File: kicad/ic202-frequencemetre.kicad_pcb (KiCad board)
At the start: 2 copper layers, 52 x 48 mm, 49 parts, among them J1 +12V IN (4 pins: 2x+12V, 2x G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, J2 RF IN, J4 LCD, Q1 2SC5551AE-TD-E, U1 AMS1117-5.0, U2 AMS1117 (ADJ), U3 MB506

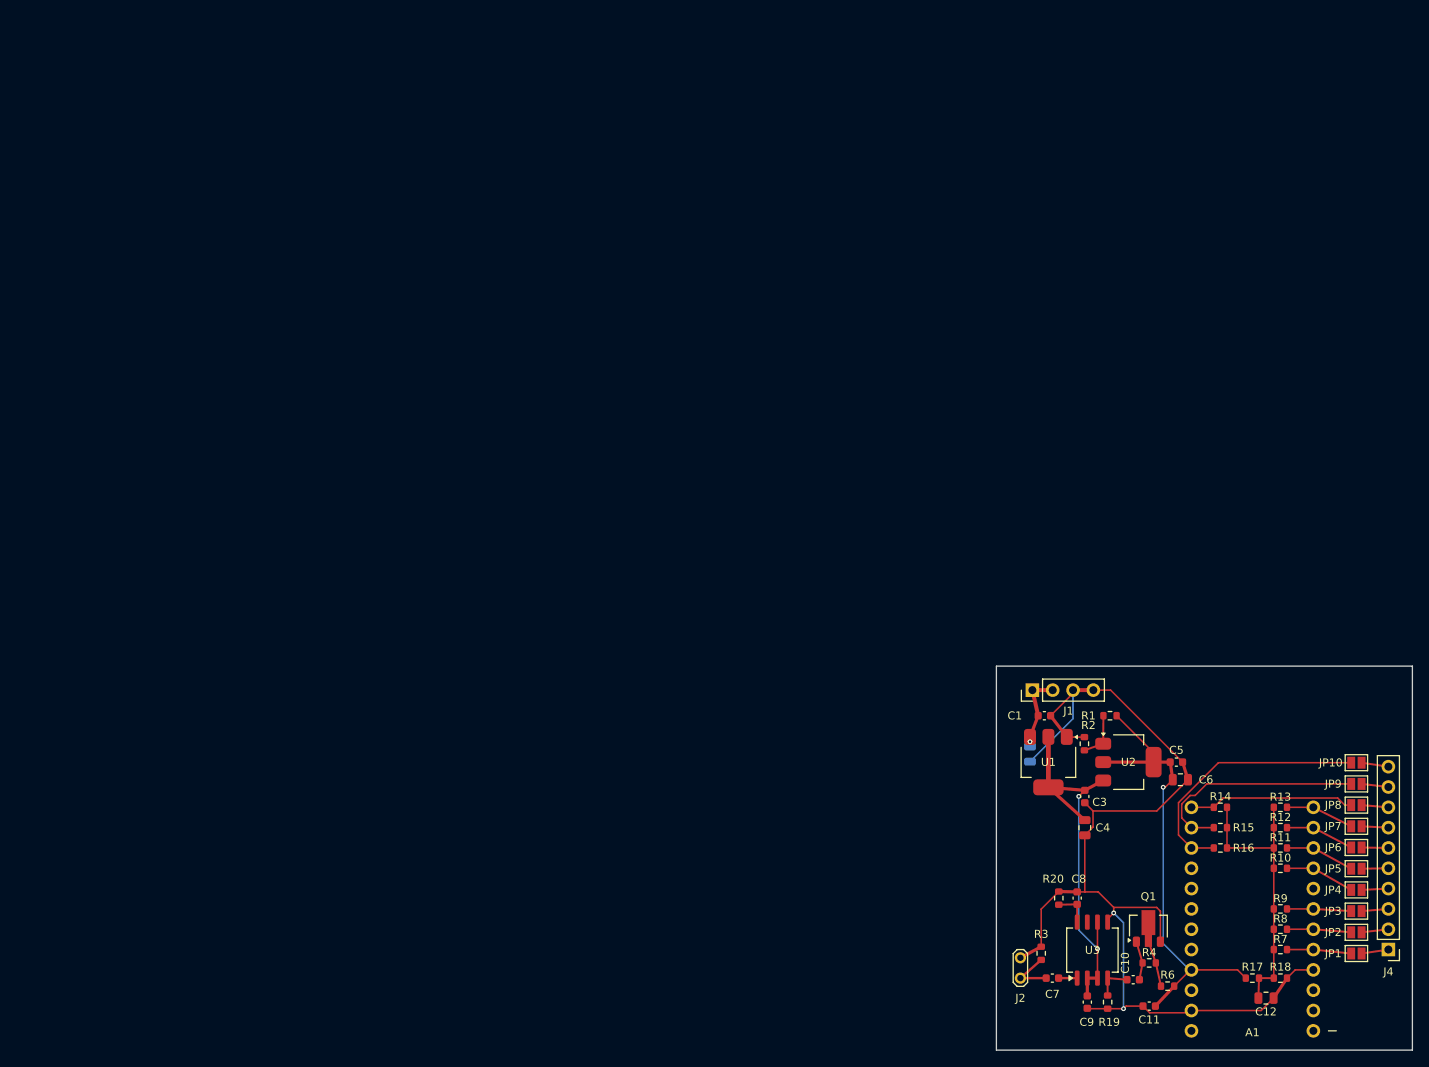
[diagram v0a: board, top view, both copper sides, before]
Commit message: Recree le PCB : placement 60x80mm + routage manuel des boucles critiques
Fichier .kicad_pcb entierement regenere depuis le schema (49 empreintes,
32 nets, 0 erreur DRC, 0 element non connecte).

Contraintes utilisateur respectees :
- contour 60 x 80 mm (portrait), composants loges dans 53,5 x 69,1 mm
- J4 (LCD) sur le bord droit, centre verticalement (y = 40 mm)
- broches de A1 (Arduino Pro Mini) paralleles a celles de J4 : A1 tourne
  a 180 deg, rangee droite face a J4. COM1/COM2/COM3 arrivent en ligne
  parfaitement droite, le reste avec un seul decalage de 2,54 mm
- J2 (entree RF) pres du bord gauche, en bas
- J1 (alimentation +12V) pres du bord haut, a gauche, broches paralleles
  au bord haut

Boucle critique J2-C7-C8-U3(broche 1)-U3(broche 8), priorite absolue :
- U3 tourne a 90 deg pour amener les broches 1 et 8 sur son cote gauche,
  face a J2 ; leur ecart de 7 mm est impose par le boitier SOIC-8
- J2, R3 et C7 alignes sur la meme ligne y = 68,5 mm que la broche 1
- C8 colle a la broche 8, sa pastille de masse tournee vers J2
- retour de masse direct C8 -> J2 broche 2 en piste 0,8 mm (6 mm)
- aire geometrique de la boucle : 46 mm2 (minimum atteignable avec
  l'ecartement du boitier et J2 contre le bord)
- doublee par un plan de masse sur les deux faces + vias de couture au
  ras de C8, R3 et R20, qui ramene la boucle HF effective a l'epaisseur
  du dielectrique sous la piste

Autres groupes "Placement" du schema :
- chemin de comptage U3(OUT)-R19-C10-R4-R6-Q1 : chaine alignee sur
  y = 68,5 mm, encombrement 8,9 x 3 mm ; D5_SIG rejoint A1 broche 8 en
  face arriere pour ne pas couper le plan sous la partie RF
- decouplages locaux colles a leur broche : C1/C2 sur U1 broche 3,
  C3/C4 sur le noeud +5V, C5/C6 sur U2 broche 2, C9 sur U3 broche 2,
  C11 pres de R6, C12 sur le pont R17/R18

Routage : manuel pour la RF, le chemin de comptage, les alimentations et
les retours de masse critiques ; Freerouting pour les 21 nets LCD/J4 et
le bus VLCD_MID. R7-R16 et le po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
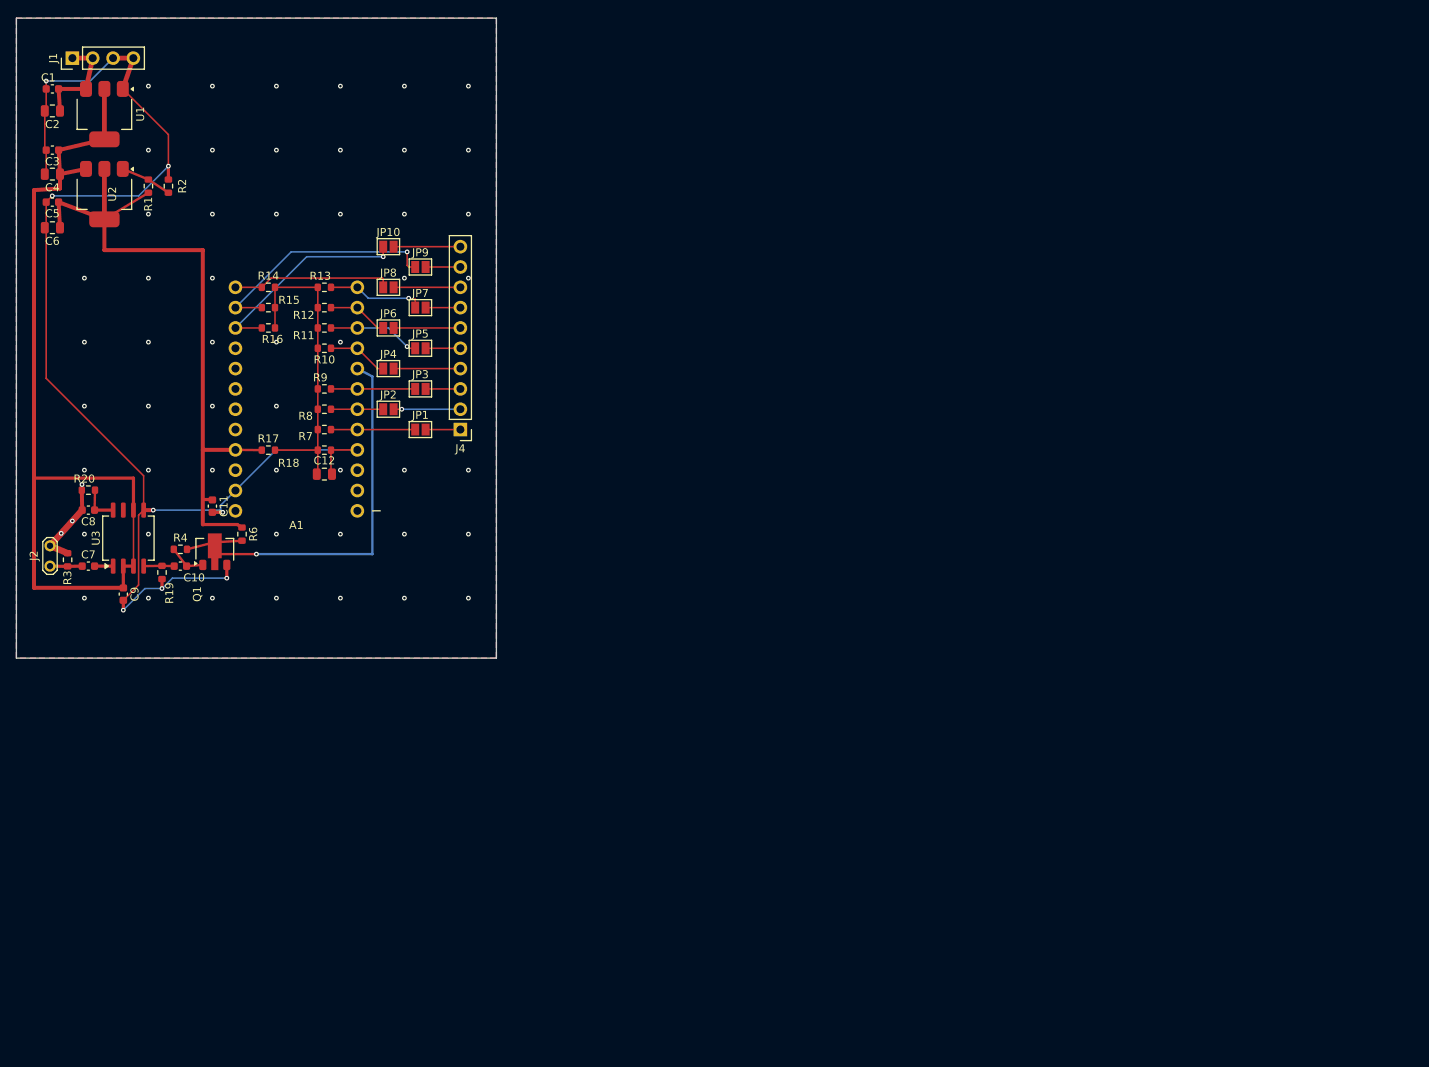
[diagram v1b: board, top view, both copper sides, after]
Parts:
- C2: moved to F.Cu
- moved C6 157.0 mm to (4.50, 26.2), turned to 180 degrees
- moved C5 157.0 mm to (4.50, 23.0), turned to 180 degrees
- moved C4 152.7 mm to (4.50, 19.5), turned to 180 degrees
- moved C3 152.3 mm to (4.50, 16.5), turned to 180 degrees
- moved C1 146.7 mm to (4.50, 8.85), turned to 180 degrees
- moved U2 146.4 mm to (11.0, 22.0), turned to -90 degrees
- moved C2 146.3 mm to (4.50, 11.6), turned to 180 degrees
- moved J1 143.7 mm to (7.00, 5.00)
- moved U1 143.1 mm to (11.0, 12.0)
- moved R17 139.6 mm to (31.5, 54.0)
- moved JP2 137.5 mm to (46.5, 48.9)
- moved JP4 137.4 mm to (46.5, 43.8)
- moved JP6 137.3 mm to (46.5, 38.7)
- moved R1 137.2 mm to (16.5, 21.0), turned to 90 degrees
- moved JP8 137.2 mm to (46.5, 33.6)
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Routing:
- net +5V: track 51.2 -> 111.9 mm, vias 2 -> 0
- net D5_SIG: track 5.86 -> 51.9 mm, vias 0 -> 1
- net GND: track 140.5 -> 182.9 mm, vias 2 -> 63
- net +3V: track 60.1 -> 92.3 mm, vias 1 -> 0
- net LCD_SEG6: track 32.8 -> 26.7 mm, vias 0 -> 1
- net J4_SEG2: track 3.35 -> 8.35 mm
- net J4_COM4: track 3.35 -> 8.35 mm
- net J4_SEG4: track 3.36 -> 8.35 mm
- net J4_COM2: track 3.37 -> 8.35 mm, vias 0 -> 1
- net J4_SEG6: track 3.39 -> 8.35 mm
- net LCD_SEG3: track 8.59 -> 12.2 mm, vias 0 -> 1
- net LCD_SEG1: track 8.69 -> 11.6 mm, vias 0 -> 1
- net +12V: track 9.86 -> 12.7 mm, vias 1 -> 0
- net RF_IN: track 6.68 -> 4.03 mm
- net VLCD_MID: track 36.6 -> 39.2 mm
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- added copper zone on B.Cu, net GND
- added copper zone on F.Cu, net GND
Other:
- board size 52 x 48 mm -> 60 x 80 mm

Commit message: Compacte le PCB : alim descendue, carte recoupee a 60 x 50 mm
Le contour 60 x 80 mm etait un point de depart a reduire, pas un cadre a
respecter : la colonne gauche avait 31,5 mm de hauteur totalement vide
(y 27,0 -> 58,5) entre la fin de l'alimentation et le debut de la partie RF.

- J1, U1, U2, C1-C6, R1 et R2 descendus de 23,67 mm en bloc : le haut de
  J1 est desormais exactement au niveau du haut de JP10 (y 1,82 mm)
- contour recoupe en haut et en bas : 60 x 50 mm au lieu de 60 x 80 mm,
  soit 1200 mm2 de carte economises ; la largeur est inchangee
- toute la geometrie translatee de -26 mm pour ramener la carte a
  l'origine ; plans de masse et vias de couture reverses sur le nouveau
  contour, 21 vias de couture hors contour supprimees
- bande morte de la colonne gauche ramenee de 31,5 mm a 7,8 mm
- emprise des composants : 53,5 x 45,5 mm (etait 53,5 x 69,1 mm)

Le bloc RF/comptage n'a pas bouge : l'aire de la boucle
J2-C7-C8-U3(broche 1)-U3(broche 8) reste a 46,3 mm2, et les pistes de
retour de masse critiques sont reposees a l'identique.

Effet de bord favorable : les regulateurs sont maintenant a mi-chemin de
leurs charges. Longueur totale routee par rail, mesuree sur le fichier :
+5V 111,9 -> 81,4 mm, +3V 92,3 -> 62,4 mm, +12V inchange a 12,7 mm (J1 et
U1 ont bouge ensemble). Le chemin U1 -> U3 passe de 77,5 a 54,1 mm.
Le decouplage suit la meme lecture des attributs Placement qu'avant, C2
(bulk) restant pres de J1 et C1 (HF) sur la broche VI de U1, tous deux
ayant suivi le bloc.

DRC : 0 violation, 0 element non connecte.

Co-Authored-By: Claude Opus 5 <noreply@anthropic.com>
Claude-Session: https://claude.ai/code/session_01V5VTDcPUUNCbvD4zhK8E2u
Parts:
- moved Q1 26.0 mm to (24.8, 40.4)
- moved R19 26.0 mm to (18.2, 43.3)
- moved R4 26.0 mm to (20.5, 40.4)
- moved JP4 26.0 mm to (46.5, 17.8)
- moved JP5 26.0 mm to (50.5, 15.3)
- moved R10 26.0 mm to (38.5, 15.3)
- moved A1 26.0 mm to (35.0, 22.9)
- moved C10 26.0 mm to (20.5, 42.5)
- moved C11 26.0 mm to (24.5, 35.0)
- moved C12 26.0 mm to (38.5, 31.0)
- moved C7 26.0 mm to (9.00, 42.5)
- moved C8 26.0 mm to (9.00, 35.5)
- moved C9 26.0 mm to (13.4, 46.0)
- moved J2 26.0 mm to (4.20, 42.5)
- moved J4 26.0 mm to (55.5, 25.4)
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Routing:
- net GND: track 182.9 -> 25.6 mm, vias 63 -> 41
- net +5V: track 111.9 -> 81.4 mm
- net +3V: track 92.3 -> 62.4 mm
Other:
- board size 60 x 80 mm -> 60 x 50 mm
